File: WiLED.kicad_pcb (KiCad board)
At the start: 2 copper layers, 50 x 50 mm, 62 parts, among them J1 Mount, J2 Mount, J3 Mount, J4 Mount, P1 Serial to USB, P2 DC In, P4 LED Out, SW1 Reset, SW2 Boot, SW3 Toggle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

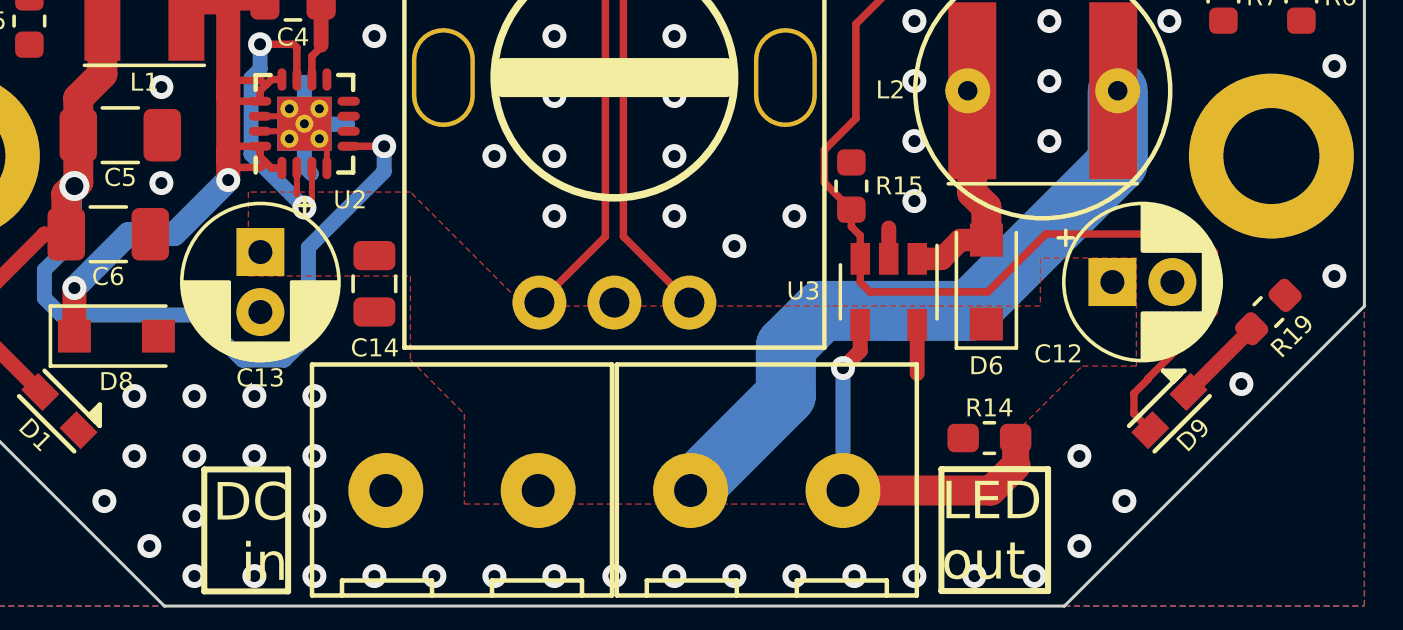
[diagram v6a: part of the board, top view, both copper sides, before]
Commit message: Nudge C12 and C13 down slightly
Moved C12 and C13 down, to make slightly more space for the screw when
fitted into the mounting hole.
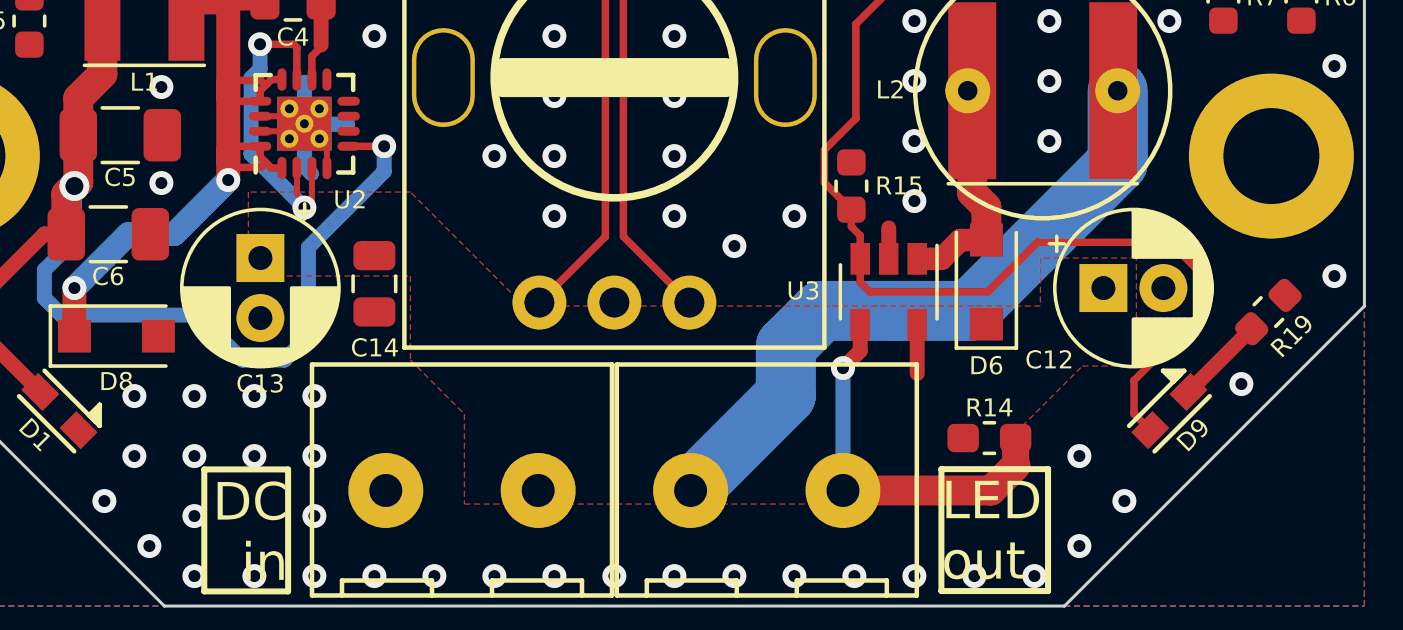
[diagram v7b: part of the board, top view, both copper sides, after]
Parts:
- moved C12 0.36 mm to (189.0, 117.0)
- moved C13 0.20 mm to (160.9, 116.0)
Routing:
- net LED_PWM: track 46.8 -> 45.4 mm
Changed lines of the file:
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@@
     (thickness 1.6)
     (drawings 66)
-    (tracks 603)
+    (tracks 601)
     (zones 0)
     (modules 62)
@@
   (title_block
     (title "WiLED ESP32 Base")
-    (date 2018-10-08)
+    (date 2018-10-09)
     (rev 3.0)
     (comment 4 "Released under the CERN Open Hardware Licence v1.2")
@@
   )
   (module Capacitor_THT:CP_Radial_D5.0mm_P2.00mm (layer F.Cu)
-    (at 160.92 115.766 270)
+    (at 160.92 115.966 270)
     (descr "CP, Radial series, Radial, pin pitch=2.00mm, , diameter=5mm, Electrolytic Capacitor")
     (tags "CP Radial series Radial pin pitch 2.00mm  diameter 5mm Electrolytic Capacitor")
@@
   )
   (module Capacitor_THT:CP_Radial_D5.0mm_P2.00mm (layer F.Cu)
-    (at 189.32 116.766)
+    (at 189.02 116.966)
     (descr "CP, Radial series, Radial, pin pitch=2.00mm, , diameter=5mm, Electrolytic Capacitor")
     (tags "CP Radial series Radial pin pitch 2.00mm  diameter 5mm Electrolytic Capacitor")
@@
   (segment (start 180.767804 111.31599) (end 179.72 112.363794) (width 0.25) (layer F.Cu) (net 20))
   (segment (start 180.77001 111.31599) (end 180.767804 111.31599) (width 0.25) (layer F.Cu) (net 20))
-  (segment (start 180.914 116.774) (end 180.914 115.994) (width 0.25) (layer F.Cu) (net 20))
-  (segment (start 181.234 117.094) (end 180.914 116.774) (width 0.25) (layer F.Cu) (net 20))
-  (segment (start 185.167002 117.094) (end 181.234 117.094) (width 0.25) (layer F.Cu) (net 20))
-  (segment (start 187.095002 115.166) (end 185.167002 117.094) (width 0.25) (layer F.Cu) (net 20))
-  (segment (start 190.039208 121.158) (end 190.039208 120.475792) (width 0.25) (layer F.Cu) (net 20))
-  (segment (start 192.12 115.166) (end 187.095002 115.166) (width 0.25) (layer F.Cu) (net 20))
-  (segment (start 190.039208 120.475792) (end 190.5 120.015) (width 0.25) (layer F.Cu) (net 20))
-  (segment (start 192.72 115.766) (end 192.12 115.166) (width 0.25) (layer F.Cu) (net 20))
-  (segment (start 190.5 120.015) (end 190.5 119.986) (width 0.25) (layer F.Cu) (net 20))
-  (segment (start 190.583604 121.702396) (end 190.039208 121.158) (width 0.25) (layer F.Cu) (net 20))
-  (segment (start 190.5 119.986) (end 192.72 117.766) (width 0.25) (layer F.Cu) (net 20))
-  (segment (start 192.72 117.766) (end 192.72 115.766) (width 0.25) (layer F.Cu) (net 20))
+  (segment (start 190.039208 121.158) (end 190.583604 121.702396) (width 0.25) (layer F.Cu) (net 20))
+  (segment (start 190.039208 120.046792) (end 190.039208 121.158) (width 0.25) (layer F.Cu) (net 20))
+  (segment (start 192.195001 117.890999) (end 190.039208 120.046792) (width 0.25) (layer F.Cu) (net 20))
+  (segment (start 192.195001 116.401999) (end 192.195001 117.890999) (width 0.25) (layer F.Cu) (net 20))
+  (segment (start 180.914 115.994) (end 180.914 116.774) (width 0.25) (layer F.Cu) (net 20))
+  (segment (start 180.914 116.774) (end 181.234 117.094) (width 0.25) (layer F.Cu) (net 20))
+  (segment (start 181.234 117.094) (end 185.167002 117.094) (width 0.25) (layer F.Cu) (net 20))
+  (segment (start 185.167002 117.094) (end 186.82 115.441002) (width 0.25) (layer F.Cu) (net 20))
+  (segment (start 186.82 115.441002) (end 191.234004 115.441002) (width 0.25) (layer F.Cu) (net 20))
+  (segment (start 191.234004 115.441002) (end 192.195001 116.401999) (width 0.25) (layer F.Cu) (net 20))
   (via (at 180.34 119.634) (size 0.8) (drill 0.4) (layers F.Cu B.Cu) (net 21))
   (segment (start 180.914 119.06) (end 180.34 119.634) (width 0.5) (layer F.Cu) (net 21))

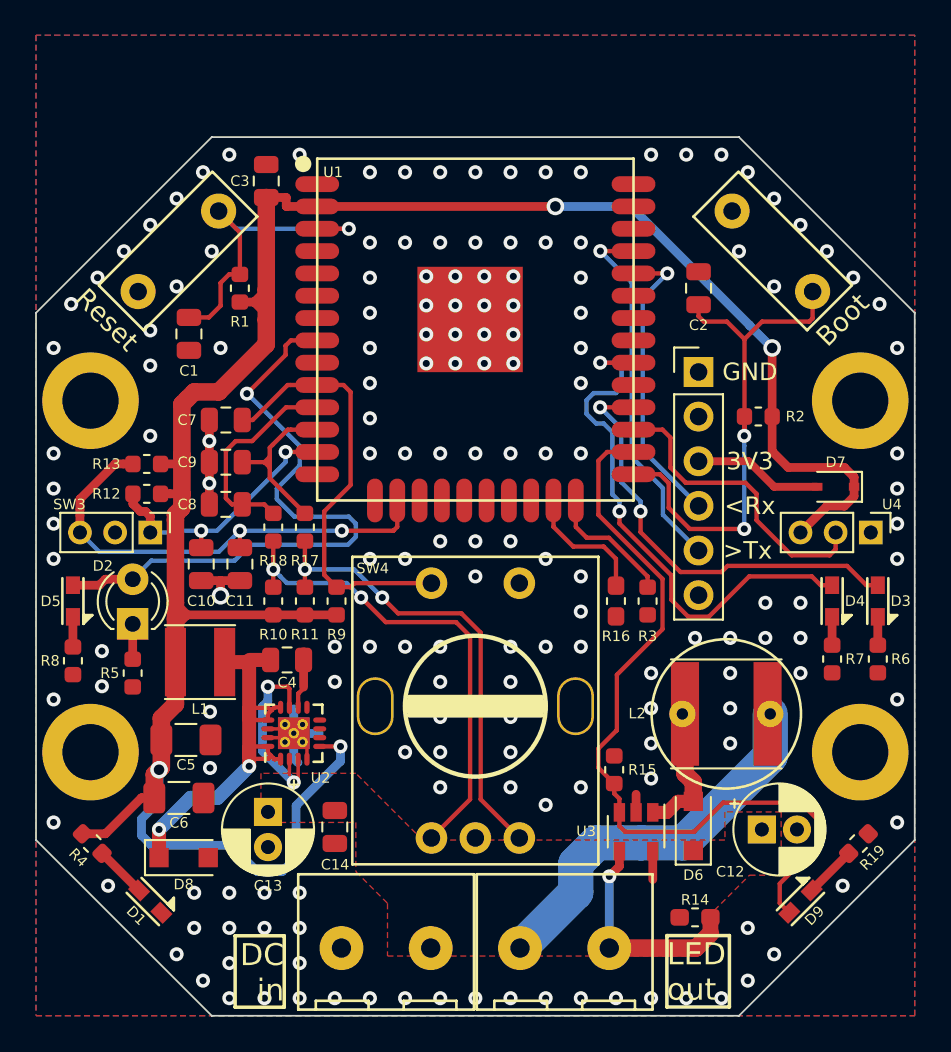
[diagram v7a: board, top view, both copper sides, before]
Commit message: Update model for pin headers, revise ground vias
Updated the footprint for the 6-pin header P1, to one with a 3D model.
Revised some ground plane vias, and re-routed some tracks to give
slightly more contiguous ground plane regions.
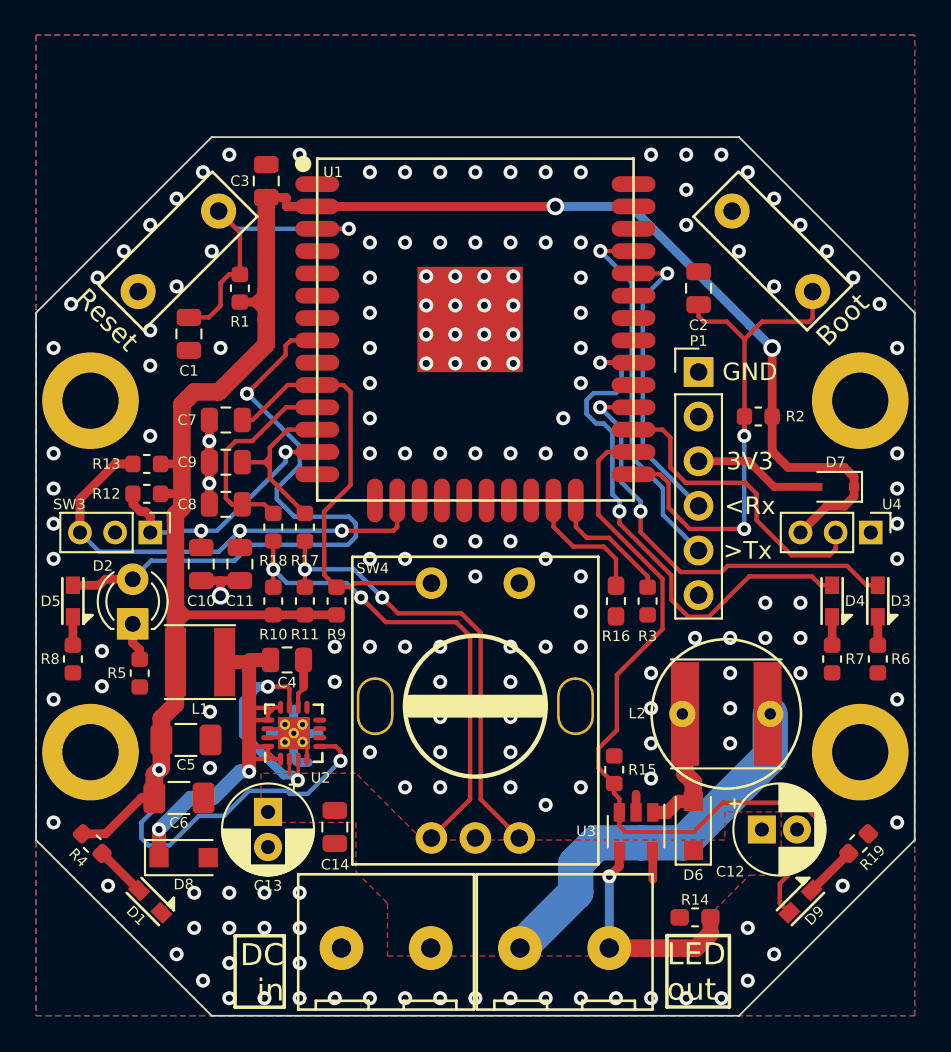
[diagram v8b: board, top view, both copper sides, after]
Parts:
- P1: footprint Pin_Headers:Pin_Header_Straight_1x06_Pitch2.54mm -> Connector_PinHeader_2.54mm:PinHeader_1x06_P2.54mm_Vertical
- moved R5 0.40 mm to (153.6, 108.1)
- moved R8 0.10 mm to (149.8, 107.3)
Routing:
- net +3V3: track 130.2 -> 127.2 mm
- net GND: track 18.5 -> 20.4 mm, vias 166 -> 170
- net RAW: track 12.5 -> 14.0 mm
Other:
- net class 3V3: trace_width 0.5 -> 0.25
- net class POWER: trace_width 0.25 -> 0.5
